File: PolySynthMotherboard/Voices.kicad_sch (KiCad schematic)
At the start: 0 parts

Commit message: ioc for standalone F411
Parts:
- added C401: 100n, symbol Device:C
- added J401: V1Header, symbol Connector:VoiceBoardConnector_18p
- added J402: V2Header, symbol Connector:VoiceBoardConnector_18p
- added J403: V3Header, symbol Connector:VoiceBoardConnector_18p
- added J404: V4Header, symbol Connector:VoiceBoardConnector_18p
- added J405: V5Header, symbol Connector:VoiceBoardConnector_18p
- added J406: V6Header, symbol Connector:VoiceBoardConnector_18p
- added R401, R402, R403, R404, R405, R406, R407, R408, R409, R410, R411, R412, R413, R414, R415: 12k, symbol Device:R_US
- added U401: TCA9548APWR, Package_SO:TSSOP-24_4.4x7.8mm_P0.65mm, symbol Interface_Expansion:TCA9548APWR
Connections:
- new net +12V: J401.2 (+12V), J402.2 (+12V), J403.2 (+12V), J404.2 (+12V), J405.2 (+12V), J406.2 (+12V)
- new net +3.3V: C401.1, R401.1, R402.1, R403.1, R404.1, R405.1, R406.1, R407.1, R408.1, R409.1, R410.1, R411.1, R412.1, R413.1, R414.1, R415.1, U401.24 (VCC)
- new net +3.3VA: J401.3 (+3v3), J402.3 (+3v3), J403.3 (+3v3), J404.3 (+3v3), J405.3 (+3v3), J406.3 (+3v3)
- new net -12V: J401.4 (-12V), J402.4 (-12V), J403.4 (-12V), J404.4 (-12V), J405.4 (-12V), J406.4 (-12V)
- new net CUTOFF_V1: J401.13 (CutoffCV)
- new net CUTOFF_V2: J402.13 (CutoffCV)
- new net CUTOFF_V3: J403.13 (CutoffCV)
- new net CUTOFF_V4: J404.13 (CutoffCV)
- new net CUTOFF_V5: J405.13 (CutoffCV)
- new net CUTOFF_V6: J406.13 (CutoffCV)
- new net FOLD_V1: J401.14 (FoldCV)
- new net FOLD_V2: J402.14 (FoldCV)
- new net FOLD_V3: J403.14 (FoldCV)
- new net FOLD_V4: J404.14 (FoldCV)
- new net FOLD_V5: J405.14 (FoldCV)
- new net FOLD_V6: J406.14 (FoldCV)
- new net FoldFirst: J401.11 (FoldFirst), J402.11 (FoldFirst), J403.11 (FoldFirst), J404.11 (FoldFirst), J405.11 (FoldFirst), J406.11 (FoldFirst)
- new net GND: C401.2, J401.1 (GND), J402.1 (GND), J403.1 (GND), J404.1 (GND), J405.1 (GND), J406.1 (GND), U401.1 (A0), U401.12 (GND), U401.2 (A1), U401.21 (A2)
- new net HPMode: J401.12 (HPMode), J402.12 (HPMode), J403.12 (HPMode), J404.12 (HPMode), J405.12 (HPMode), J406.12 (HPMode)
- new net I2C_MUX_RST: R405.2, U401.3 (~{RESET})
- new net LVL1_V1: J401.10 (PWM1), J401.8 (L1)
- new net LVL1_V2: J402.10 (PWM1), J402.8 (L1)
- new net LVL1_V3: J403.10 (PWM1), J403.8 (L1)
- new net LVL1_V4: J404.10 (PWM1), J404.8 (L1)
- new net LVL1_V5: J405.10 (PWM1), J405.8 (L1)
- new net LVL1_V6: J406.10 (PWM1), J406.8 (L1)
- new net LVL2_V1: J401.7 (L2), J401.9 (PWM2)
- new net LVL2_V2: J402.7 (L2), J402.9 (PWM2)
- new net LVL2_V3: J403.7 (L2), J403.9 (PWM2)
- new net LVL2_V4: J404.7 (L2), J404.9 (PWM2)
- new net LVL2_V5: J405.7 (L2), J405.9 (PWM2)
- new net LVL2_V6: J406.7 (L2), J406.9 (PWM2)
- new net POTS_SCL: R401.2, U401.22 (SCL)
- new net POTS_SDA: R402.2, U401.23 (SDA)
- new net SCL_V1: J401.18 (SCL), R403.2, U401.5 (SC0)
- new net SCL_V2: J402.18 (SCL), R407.2, U401.7 (SC1)
- new net SCL_V3: J403.18 (SCL), R409.2, U401.9 (SC2)
- new net SCL_V4: J404.18 (SCL), R411.2, U401.11 (SC3)
- new net SCL_V5: J405.18 (SCL), R413.2, U401.14 (SC4)
- new net SCL_V6: J406.18 (SCL), R415.2, U401.16 (SC5)
- new net SDA_V1: J401.17 (SDA), R404.2, U401.4 (SD0)
- new net SDA_V2: J402.17 (SDA), R406.2, U401.6 (SD1)
- new net SDA_V3: J403.17 (SDA), R408.2, U401.8 (SD2)
- new net SDA_V4: J404.17 (SDA), R410.2, U401.10 (SD3)
- new net SDA_V5: J405.17 (SDA), R412.2, U401.13 (SD4)
- new net SDA_V6: J406.17 (SDA), R414.2, U401.15 (SD5)
- new net V1_CLK1: J401.6 (CLK1)
- new net V1_CLK2: J401.5 (CLK2)
- new net V1_OUT: J401.16 (VoiceOut)
- new net V2_CLK1: J402.6 (CLK1)
- new net V2_CLK2: J402.5 (CLK2)
- new net V2_OUT: J402.16 (VoiceOut)
- new net V3_CLK1: J403.6 (CLK1)
- new net V3_CLK2: J403.5 (CLK2)
- new net V3_OUT: J403.16 (VoiceOut)
- new net V4_CLK1: J404.6 (CLK1)
- new net V4_CLK2: J404.5 (CLK2)
- new net V4_OUT: J404.16 (VoiceOut)
- new net V5_CLK1: J405.6 (CLK1)
- new net V5_CLK2: J405.5 (CLK2)
- new net V5_OUT: J405.16 (VoiceOut)
- new net V6_CLK1: J406.6 (CLK1)
- new net V6_CLK2: J406.5 (CLK2)
- new net V6_OUT: J406.16 (VoiceOut)
- new net VCA_V1: J401.15 (VCACV)
- new net VCA_V2: J402.15 (VCACV)
- new net VCA_V3: J403.15 (VCACV)
- new net VCA_V4: J404.15 (VCACV)
- new net VCA_V5: J405.15 (VCACV)
- new net VCA_V6: J406.15 (VCACV)
- no-connect marks 0 -> 4
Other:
- note added: "I2C Multiplexer"
- note added: "Voice Board Connectors"

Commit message: power supply/ output circuits
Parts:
- C401: footprint (none) -> Capacitor_SMD:C_0805_2012Metric
- J401, J402, J403, J404, J405, J406: footprint (none) -> Connector_PinSocket_2.54mm:PinSocket_1x18_P2.54mm_Vertical
- R401, R402, R403, R404, R405, R406, R407, R408, R409, R410, R411, R412, R413, R414, R415: footprint (none) -> PCM_Resistor_SMD_AKL:R_0805_2012Metric
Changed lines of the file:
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@@
       (effects (font (size 1.27 1.27)) (justify left))
     )
-    (property "Footprint" "" (at 219.202 115.57 90)
+    (property "Footprint" "PCM_Resistor_SMD_AKL:R_0805_2012Metric" (at 219.202 115.57 90)
       (effects (font (size 1.27 1.27)) hide)
     )
@@
       (effects (font (size 1.27 1.27)) (justify left))
     )
-    (property "Footprint" "" (at 74.168 111.252 90)
+    (property "Footprint" "PCM_Resistor_SMD_AKL:R_0805_2012Metric" (at 74.168 111.252 90)
       (effects (font (size 1.27 1.27)) hide)
     )
@@
       (effects (font (size 1.27 1.27)) (justify left))
     )
-    (property "Footprint" "" (at 228.346 172.466 90)
+    (property "Footprint" "PCM_Resistor_SMD_AKL:R_0805_2012Metric" (at 228.346 172.466 90)
       (effects (font (size 1.27 1.27)) hide)
     )
@@
       (effects (font (size 1.27 1.27)) (justify left))
     )
-    (property "Footprint" "" (at 281.94 116.078 90)
+    (property "Footprint" "PCM_Resistor_SMD_AKL:R_0805_2012Metric" (at 281.94 116.078 90)
       (effects (font (size 1.27 1.27)) hide)
     )
@@
       (effects (font (size 1.27 1.27)) (justify left))
     )
-    (property "Footprint" "" (at 63.246 111.506 90)
+    (property "Footprint" "PCM_Resistor_SMD_AKL:R_0805_2012Metric" (at 63.246 111.506 90)
       (effects (font (size 1.27 1.27)) hide)
     )
@@
       (effects (font (size 1.27 1.27)) (justify left))
     )
-    (property "Footprint" "" (at 353.06 172.72 90)
+    (property "Footprint" "PCM_Resistor_SMD_AKL:R_0805_2012Metric" (at 353.06 172.72 90)
       (effects (font (size 1.27 1.27)) hide)
     )
@@
       (effects (font (size 1.27 1.27)) (justify left))
     )
-    (property "Footprint" "" (at 235.966 172.466 90)
+    (property "Footprint" "PCM_Resistor_SMD_AKL:R_0805_2012Metric" (at 235.966 172.466 90)
       (effects (font (size 1.27 1.27)) hide)
     )
@@
       (effects (font (size 1.27 1.27)) (justify right))
     )
-    (property "Footprint" "" (at 89.1032 112.522 0)
+    (property "Footprint" "Capacitor_SMD:C_0805_2012Metric" (at 89.1032 112.522 0)
       (effects (font (size 1.27 1.27)) hide)
     )
@@
       (effects (font (size 1.27 1.27)))
     )
-    (property "Footprint" "" (at 310.134 102.108 0)
+    (property "Footprint" "Connector_PinSocket_2.54mm:PinSocket_1x18_P2.54mm_Vertical" (at 310.134 102.108 0)
       (effects (font (size 1.27 1.27)) hide)
     )
@@
       (effects (font (size 1.27 1.27)) (justify left))
     )
-    (property "Footprint" "" (at 289.56 116.078 90)
+    (property "Footprint" "PCM_Resistor_SMD_AKL:R_0805_2012Metric" (at 289.56 116.078 90)
       (effects (font (size 1.27 1.27)) hide)
     )
@@
       (effects (font (size 1.27 1.27)))
     )
-    (property "Footprint" "" (at 319.278 159.004 0)
+    (property "Footprint" "Connector_PinSocket_2.54mm:PinSocket_1x18_P2.54mm_Vertical" (at 319.278 159.004 0)
       (effects (font (size 1.27 1.27)) hide)
     )
@@
       (effects (font (size 1.27 1.27)))
     )
-    (property "Footprint" "" (at 248.158 102.362 0)
+    (property "Footprint" "Connector_PinSocket_2.54mm:PinSocket_1x18_P2.54mm_Vertical" (at 248.158 102.362 0)
       (effects (font (size 1.27 1.27)) hide)
     )
@@
       (effects (font (size 1.27 1.27)) (justify left))
     )
-    (property "Footprint" "" (at 360.68 172.72 90)
+    (property "Footprint" "PCM_Resistor_SMD_AKL:R_0805_2012Metric" (at 360.68 172.72 90)
       (effects (font (size 1.27 1.27)) hide)
     )
@@
       (effects (font (size 1.27 1.27)) (justify left))
     )
-    (property "Footprint" "" (at 298.704 172.974 90)
+    (property "Footprint" "PCM_Resistor_SMD_AKL:R_0805_2012Metric" (at 298.704 172.974 90)
       (effects (font (size 1.27 1.27)) hide)
     )
@@
       (effects (font (size 1.27 1.27)))
     )
-    (property "Footprint" "" (at 194.564 158.75 0)
+    (property "Footprint" "Connector_PinSocket_2.54mm:PinSocket_1x18_P2.54mm_Vertical" (at 194.564 158.75 0)
       (effects (font (size 1.27 1.27)) hide)
     )
@@
       (effects (font (size 1.27 1.27)) (justify left))
     )
-    (property "Footprint" "" (at 226.822 115.57 90)
+    (property "Footprint" "PCM_Resistor_SMD_AKL:R_0805_2012Metric" (at 226.822 115.57 90)
       (effects (font (size 1.27 1.27)) hide)
     )
@@
       (effects (font (size 1.27 1.27)))
     )
-    (property "Footprint" "" (at 257.302 159.258 0)
+    (property "Footprint" "Connector_PinSocket_2.54mm:PinSocket_1x18_P2.54mm_Vertical" (at 257.302 159.258 0)
       (effects (font (size 1.27 1.27)) hide)
     )
@@
       (effects (font (size 1.27 1.27)))
     )
-    (property "Footprint" "" (at 185.42 101.854 0)
+    (property "Footprint" "Connector_PinSocket_2.54mm:PinSocket_1x18_P2.54mm_Vertical" (at 185.42 101.854 0)
       (effects (font (size 1.27 1.27)) hide)
     )
@@
       (effects (font (size 1.27 1.27)) (justify left))
     )
-    (property "Footprint" "" (at 343.916 115.824 90)
+    (property "Footprint" "PCM_Resistor_SMD_AKL:R_0805_2012Metric" (at 343.916 115.824 90)
       (effects (font (size 1.27 1.27)) hide)
     )
@@
       (effects (font (size 1.27 1.27)) (justify left))
     )
-    (property "Footprint" "" (at 351.536 115.824 90)
+    (property "Footprint" "PCM_Resistor_SMD_AKL:R_0805_2012Metric" (at 351.536 115.824 90)
       (effects (font (size 1.27 1.27)) hide)
     )
@@
       (effects (font (size 1.27 1.27)) (justify left))
     )
-    (property "Footprint" "" (at 67.31 135.89 90)
+    (property "Footprint" "PCM_Resistor_SMD_AKL:R_0805_2012Metric" (at 67.31 135.89 90)
       (effects (font (size 1.27 1.27)) hide)
     )
@@
       (effects (font (size 1.27 1.27)) (justify left))
     )
-    (property "Footprint" "" (at 291.084 172.974 90)
-      (effects (font (size 1.27 1.27)) hide)
-    )
+    (property "Footprint" "PCM_Resistor_SMD_AKL:R_0805_2012Metric" (at 291.084 172.974 90)
+      (effects (font (size 1.27 1.27)) hide)
+    )

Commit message: new voice board proj
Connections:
- net +3.3VA is gone; now on net +3.3V: J401.3 (+3v3), J402.3 (+3v3), J403.3 (+3v3), J404.3 (+3v3), J405.3 (+3v3), J406.3 (+3v3)
- net I2C_MUX_RST renamed I2C_MUX_LST

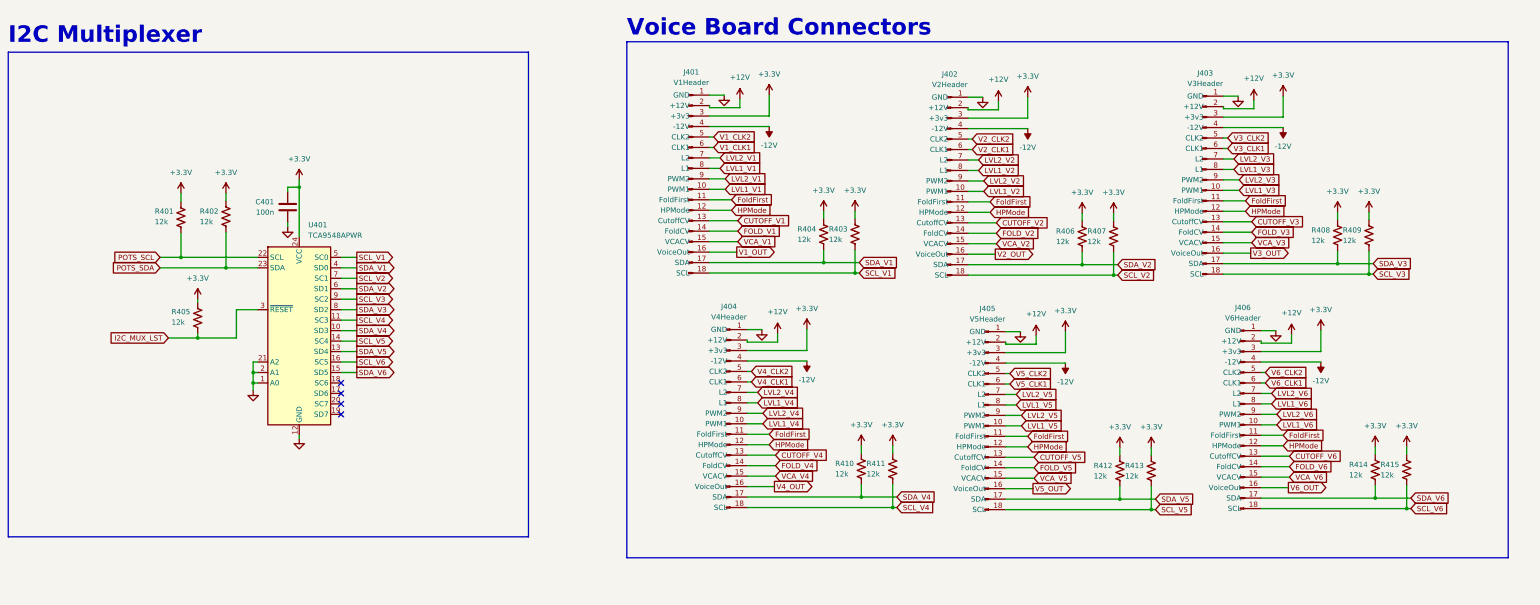
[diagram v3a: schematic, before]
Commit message: op-amp layout improved
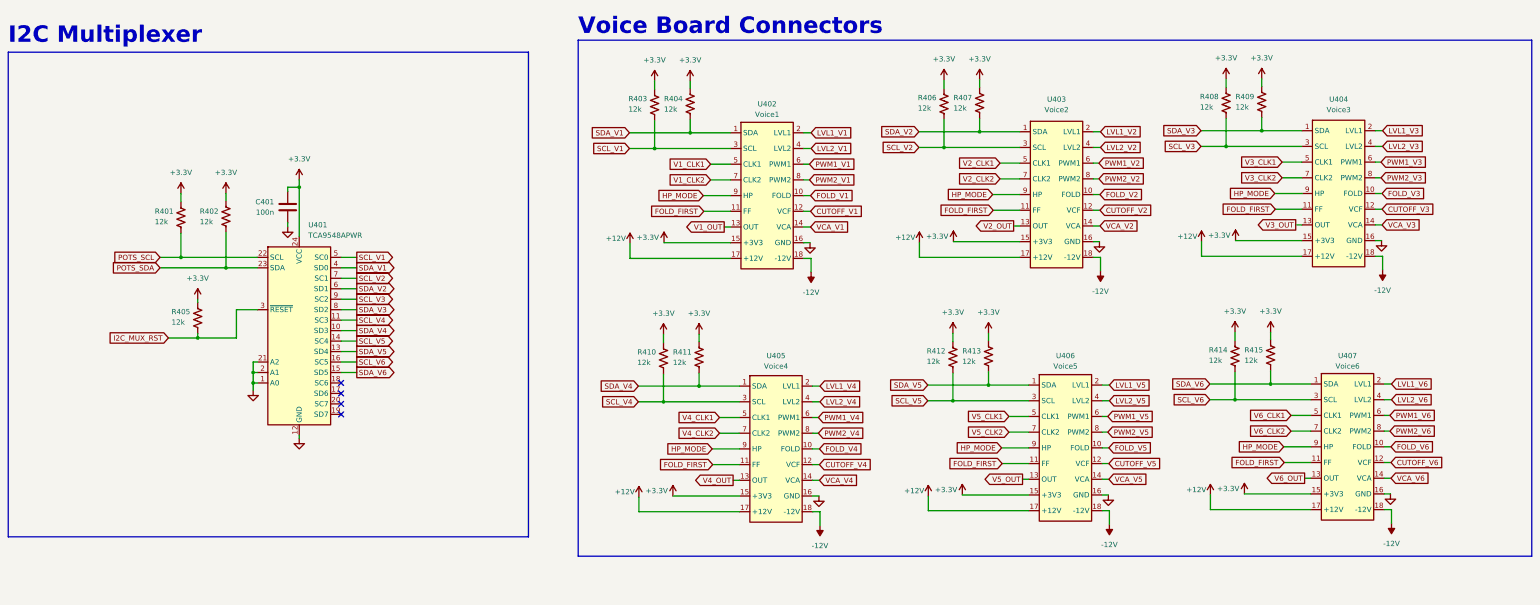
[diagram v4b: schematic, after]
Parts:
- removed J401: V1Header, Connector_PinSocket_2.54mm:PinSocket_1x18_P2.54mm_Vertical, symbol Connector:VoiceBoardConnector_18p
- removed J402: V2Header, Connector_PinSocket_2.54mm:PinSocket_1x18_P2.54mm_Vertical, symbol Connector:VoiceBoardConnector_18p
- removed J403: V3Header, Connector_PinSocket_2.54mm:PinSocket_1x18_P2.54mm_Vertical, symbol Connector:VoiceBoardConnector_18p
- removed J404: V4Header, Connector_PinSocket_2.54mm:PinSocket_1x18_P2.54mm_Vertical, symbol Connector:VoiceBoardConnector_18p
- removed J405: V5Header, Connector_PinSocket_2.54mm:PinSocket_1x18_P2.54mm_Vertical, symbol Connector:VoiceBoardConnector_18p
- removed J406: V6Header, Connector_PinSocket_2.54mm:PinSocket_1x18_P2.54mm_Vertical, symbol Connector:VoiceBoardConnector_18p
- added U402: Voice1, Connector_PinHeader_2.54mm:PinHeader_2x09_P2.54mm_Vertical, symbol Connector_Audio:VoiceBoardConn_18P_254P
- added U403: Voice2, Connector_PinHeader_2.54mm:PinHeader_2x09_P2.54mm_Vertical, symbol Connector_Audio:VoiceBoardConn_18P_254P
- added U404: Voice3, Connector_PinHeader_2.54mm:PinHeader_2x09_P2.54mm_Vertical, symbol Connector_Audio:VoiceBoardConn_18P_254P
- added U405: Voice4, Connector_PinHeader_2.54mm:PinHeader_2x09_P2.54mm_Vertical, symbol Connector_Audio:VoiceBoardConn_18P_254P
- added U406: Voice5, Connector_PinHeader_2.54mm:PinHeader_2x09_P2.54mm_Vertical, symbol Connector_Audio:VoiceBoardConn_18P_254P
- added U407: Voice6, Connector_PinHeader_2.54mm:PinHeader_2x09_P2.54mm_Vertical, symbol Connector_Audio:VoiceBoardConn_18P_254P
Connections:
- net +12V: now also U402.17 (+12V), U403.17 (+12V), U404.17 (+12V), U405.17 (+12V), U406.17 (+12V), U407.17 (+12V)
- net +3.3V: now also U402.15 (+3V3), U403.15 (+3V3), U404.15 (+3V3), U405.15 (+3V3), U406.15 (+3V3), U407.15 (+3V3)
- net -12V: now also U402.18 (-12V), U403.18 (-12V), U404.18 (-12V), U405.18 (-12V), U406.18 (-12V), U407.18 (-12V)
- net CUTOFF_V1: now also U402.12 (VCF)
- net CUTOFF_V2: now also U403.12 (VCF)
- net CUTOFF_V3: now also U404.12 (VCF)
- net CUTOFF_V4: now also U405.12 (VCF)
- net CUTOFF_V5: now also U406.12 (VCF)
- net CUTOFF_V6: now also U407.12 (VCF)
- net FOLD_V1: now also U402.10 (FOLD)
- net FOLD_V2: now also U403.10 (FOLD)
- net FOLD_V3: now also U404.10 (FOLD)
- net FOLD_V4: now also U405.10 (FOLD)
- net FOLD_V5: now also U406.10 (FOLD)
- net FOLD_V6: now also U407.10 (FOLD)
- net GND: now also U402.16 (GND), U403.16 (GND), U404.16 (GND), U405.16 (GND), U406.16 (GND), U407.16 (GND)
- net LVL1_V1: now also U402.2 (LVL1)
- net LVL1_V2: now also U403.2 (LVL1)
- net LVL1_V3: now also U404.2 (LVL1)
- net LVL1_V4: now also U405.2 (LVL1)
- net LVL1_V5: now also U406.2 (LVL1)
- net LVL1_V6: now also U407.2 (LVL1)
- net LVL2_V1: now also U402.4 (LVL2)
- net LVL2_V2: now also U403.4 (LVL2)
- net LVL2_V3: now also U404.4 (LVL2)
- net LVL2_V4: now also U405.4 (LVL2)
- net LVL2_V5: now also U406.4 (LVL2)
- net LVL2_V6: now also U407.4 (LVL2)
- net SCL_V1: now also U402.3 (SCL)
- net SCL_V2: now also R406.2, U403.3 (SCL); no longer R407.2
- net SCL_V3: now also R408.2, U404.3 (SCL); no longer R409.2
- net SCL_V4: now also R410.2, U405.3 (SCL); no longer R411.2
- net SCL_V5: now also R412.2, U406.3 (SCL); no longer R413.2
- net SCL_V6: now also R414.2, U407.3 (SCL); no longer R415.2
- net SDA_V1: now also U402.1 (SDA)
- net SDA_V2: now also R407.2, U403.1 (SDA); no longer R406.2
- net SDA_V3: now also R409.2, U404.1 (SDA); no longer R408.2
- net SDA_V4: now also R411.2, U405.1 (SDA); no longer R410.2
- net SDA_V5: now also R413.2, U406.1 (SDA); no longer R412.2
- net SDA_V6: now also R415.2, U407.1 (SDA); no longer R414.2
- net V1_CLK1: now also U402.5 (CLK1)
- net V1_CLK2: now also U402.7 (CLK2)
- net V1_OUT: now also U402.13 (OUT)
- net V2_CLK1: now also U403.5 (CLK1)
- net V2_CLK2: now also U403.7 (CLK2)
- net V2_OUT: now also U403.13 (OUT)
- net V3_CLK1: now also U404.5 (CLK1)
- net V3_CLK2: now also U404.7 (CLK2)
- net V3_OUT: now also U404.13 (OUT)
- net V4_CLK1: now also U405.5 (CLK1)
- net V4_CLK2: now also U405.7 (CLK2)
- net V4_OUT: now also U405.13 (OUT)
- net V5_CLK1: now also U406.5 (CLK1)
- net V5_CLK2: now also U406.7 (CLK2)
- net V5_OUT: now also U406.13 (OUT)
- net V6_CLK1: now also U407.5 (CLK1)
- net V6_CLK2: now also U407.7 (CLK2)
- net V6_OUT: now also U407.13 (OUT)
- net VCA_V1: now also U402.14 (VCA)
- net VCA_V2: now also U403.14 (VCA)
- net VCA_V3: now also U404.14 (VCA)
- net VCA_V4: now also U405.14 (VCA)
- net VCA_V5: now also U406.14 (VCA)
- net VCA_V6: now also U407.14 (VCA)
- net I2C_MUX_LST renamed I2C_MUX_RST
- new net FOLD_FIRST: U402.11 (FF), U403.11 (FF), U404.11 (FF), U405.11 (FF), U406.11 (FF), U407.11 (FF)
- new net HP_MODE: U402.9 (HP), U403.9 (HP), U404.9 (HP), U405.9 (HP), U406.9 (HP), U407.9 (HP)
- new net PWM1_V1: U402.6 (PWM1)
- new net PWM1_V2: U403.6 (PWM1)
- new net PWM1_V3: U404.6 (PWM1)
- new net PWM1_V4: U405.6 (PWM1)
- new net PWM1_V5: U406.6 (PWM1)
- new net PWM1_V6: U407.6 (PWM1)
- new net PWM2_V1: U402.8 (PWM2)
- new net PWM2_V2: U403.8 (PWM2)
- new net PWM2_V3: U404.8 (PWM2)
- new net PWM2_V4: U405.8 (PWM2)
- new net PWM2_V5: U406.8 (PWM2)
- new net PWM2_V6: U407.8 (PWM2)
